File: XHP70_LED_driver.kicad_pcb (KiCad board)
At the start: 2 copper layers, 17 x 17 mm, 24 parts, among them U1 TPS61088, U2 INA181

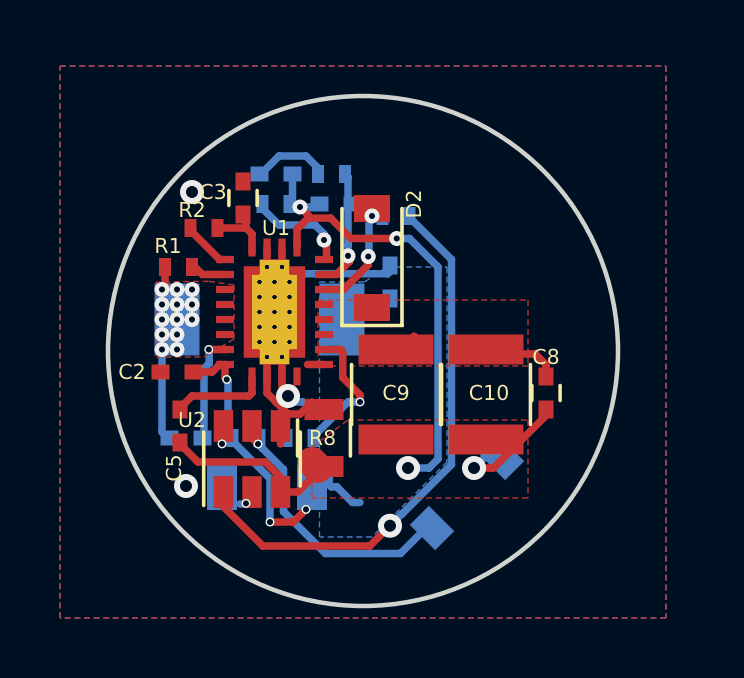
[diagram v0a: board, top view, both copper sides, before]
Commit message: added microcontroller
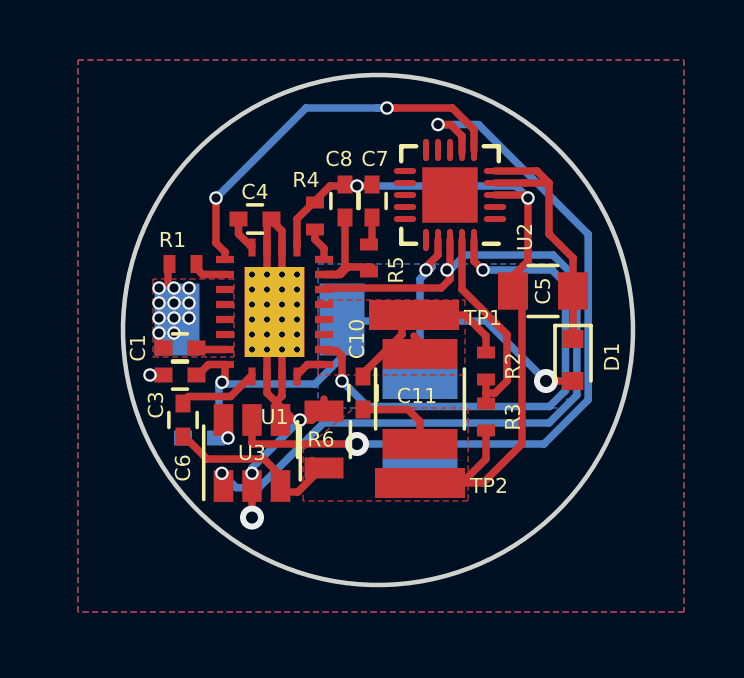
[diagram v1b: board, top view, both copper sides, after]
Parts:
- removed D2: D_Zener, Diodes_SMD:D_SOD-123
- removed R7: 10k, Resistors_SMD:R_0402_NoSilk
- removed R8: 12m, Resistors_SMD:R_0805
- added TP1: TestPoint, Misc:flashlight_batt, F.Cu at (104.4, 57.1)
- added TP2: TestPoint, Misc:flashlight_batt, F.Cu at (104.6, 62.7)
- added U3: INA181, TO_SOT_Packages_SMD:SOT-23-6, F.Cu at (99.0, 61.7)
- C1: value 10u -> 100n; footprint Capacitors_SMD:C_1206 -> Capacitors_SMD:C_0402; moved to F.Cu
- C10: value 100u -> 100n; footprint Capacitors_SMD:C_1210 -> Capacitors_SMD:C_0402
- C11: value 10u -> 100u; footprint Capacitors_SMD:C_0402 -> Capacitors_SMD:C_1210; moved to F.Cu
- C2: value 100n -> 10u; footprint Capacitors_SMD:C_0402_NoSilk -> Capacitors_SMD:C_1210; moved to B.Cu
- C3: value 10u -> 100n
- C4: value 100n -> 10u; moved to F.Cu
- C5: value 10n -> 47u; footprint Capacitors_SMD:C_0402_NoSilk -> Capacitors_SMD:C_0805
- C6: value C -> 10n; footprint Capacitors_SMD:C_0402_NoSilk -> Capacitors_SMD:C_0402; moved to F.Cu
- C7: footprint Capacitors_SMD:C_0402_NoSilk -> Capacitors_SMD:C_0402; moved to F.Cu
- C8: value 100n -> C
- C9: value 100u -> 10u; footprint Capacitors_SMD:C_1210 -> Capacitors_SMD:C_0402; moved to B.Cu
- D1: value D_Zener -> D_Schottky; footprint Diodes_SMD:D_SOD-123 -> Diodes_SMD:D_SOD-523; moved to F.Cu
- R3: value 10k -> 100k; moved to F.Cu
- R4: moved to F.Cu
- R5: value 100k -> R; moved to F.Cu
- R6: value R -> 12m; footprint Resistors_SMD:R_0402_NoSilk -> Resistors_SMD:R_0805; moved to F.Cu
- U2: value INA181 -> ATtiny816_(QFN20); footprint TO_SOT_Packages_SMD:SOT-23-6 -> Housings_DFN_QFN:UQFN-20-1EP_3x3mm_Pitch0.4mm
- moved C5 12.9 mm to (108.7, 56.3), turned to 0 degrees
- moved U2 11.0 mm to (105.6, 53.1), turned to 180 degrees
- moved R2 10.5 mm to (106.8, 58.8), turned to 90 degrees
- moved C8 9.27 mm to (102.1, 53.3), turned to 270 degrees
- moved R6 8.85 mm to (101.4, 61.2), turned to 90 degrees
- moved C6 8.77 mm to (96.7, 60.6), turned to 90 degrees
- moved C2 8.32 mm to (104.6, 60.9), turned to 90 degrees
- moved R3 8.03 mm to (106.8, 60.5), turned to 90 degrees
- moved C4 7.65 mm to (99.1, 53.9)
- moved R4 7.42 mm to (101.1, 53.8), turned to 270 degrees
- moved C9 6.71 mm to (97.2, 61.2), turned to 0 degrees
- moved C3 6.26 mm to (96.6, 59.1), turned to 0 degrees
- moved D1 5.67 mm to (109.7, 58.6), turned to 270 degrees
- moved C1 5.44 mm to (96.6, 58.2), turned to 180 degrees
- moved C10 4.10 mm to (102.7, 59.7)
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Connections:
- C1 pad 1: GND -> Net-(C1-Pad1)
- C1 pad 2: +BATT -> Net-(C1-Pad2)
- C11 pad 1: GND -> /LED_K
- C11 pad 2: +BATT -> /LED_A
- C3 pad 2: Net-(C3-Pad2) -> +BATT
- C4 pad 1: Net-(C4-Pad1) -> GND
- C8 pad 2: /LED_A -> Net-(C8-Pad2)
- C9 pad 1: /LED_K -> GND
- C9 pad 2: /LED_A -> +BATT
- D1 pad 1: Net-(D1-Pad1) -> Net-(C5-Pad2)
- D1 pad 2: /LED_K -> +BATT
- L1 pad 1: Net-(C4-Pad2) -> Net-(C1-Pad2)
- R1 pad 2: Net-(C4-Pad2) -> Net-(C1-Pad2)
- R2 pad 1: Net-(R2-Pad1) -> /ADC_VOUT
- R2 pad 2: Net-(C3-Pad2) -> /LED_A
- R3 pad 1: Net-(D1-Pad1) -> /LED_K
- R3 pad 2: +BATT -> /ADC_VOUT
- R4 pad 1: GND -> /LED_K
- R5 pad 1: /LED_K -> Net-(C8-Pad2)
- R5 pad 2: Net-(R5-Pad2) -> Net-(C7-Pad2)
- R6 pad 1: Net-(C7-Pad2) -> /LED_K
- R6 pad 2: Net-(C6-Pad2) -> GND
- U1 pad 1: Net-(C3-Pad2) -> Net-(C4-Pad2)
- U1 pad 10: Net-(C5-Pad2) -> Net-(C6-Pad2)
- U1 pad 13: Net-(R4-Pad2) -> /MODE
- U1 pad 17: Net-(D2-Pad2) -> /ADC_IOUT
- U1 pad 18: Net-(C7-Pad2) -> Net-(C8-Pad2)
- U1 pad 19: Net-(R5-Pad2) -> Net-(R4-Pad2)
- U1 pad 2: Net-(R2-Pad1) -> /ENABLE
- U1 pad 4: Net-(C4-Pad2) -> Net-(C1-Pad2)
- U1 pad 5: Net-(C4-Pad2) -> Net-(C1-Pad2)
- U1 pad 6: Net-(C4-Pad2) -> Net-(C1-Pad2)
- U1 pad 7: Net-(C4-Pad2) -> Net-(C1-Pad2)
- U1 pad 8: Net-(C4-Pad1) -> Net-(C1-Pad1)
- U2 pad 2: GND -> Net-(U2-Pad2)
- U2 pad 4: GND -> Net-(C5-Pad2)
- U2 pad 5: Net-(D1-Pad1) -> Net-(C5-Pad2)
- U2 pad 6: +BATT -> /ENABLE
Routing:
- net /ADC_IOUT: track 0.00 -> 28.0 mm, vias 0 -> 2
- net /DAC_OUT: track 0.00 -> 26.2 mm, vias 0 -> 2
- net Net-(U2-Pad1): track 18.7 -> 0.00 mm, vias 1 -> 0
- net /MODE: track 0.00 -> 17.1 mm, vias 0 -> 2
- net +BATT: track 10.9 -> 23.9 mm
- net /ENABLE: track 0.00 -> 13.0 mm, vias 0 -> 2
- net Net-(D1-Pad1): track 9.78 -> 0.00 mm, vias 1 -> 0
- net /LED_K: track 27.2 -> 36.2 mm, vias 4 -> 2
- net /ADC_VOUT: track 0.00 -> 6.94 mm
- net Net-(C5-Pad2): track 3.16 -> 9.20 mm
- net Net-(C8-Pad2): track 0.00 -> 4.01 mm
- net Net-(C7-Pad2): track 4.39 -> 0.40 mm, vias 1 -> 0
- net Net-(D2-Pad2): track 3.73 -> 0.00 mm, vias 2 -> 0
- net Net-(C4-Pad1): track 3.56 -> 0.00 mm, vias 1 -> 0
- net Net-(R4-Pad2): track 4.67 -> 1.17 mm, vias 1 -> 0
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- added copper zone on F.Cu, net Net-(C1-Pad2)
- removed copper zone on F.Cu, net Net-(C4-Pad2)
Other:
- net class Default: clearance 0.2 -> 0.127
- rule trace_clearance: 0.2 -> 0.127
- rule trace_min: 0.2 -> 0.0889
- rule via_min_size: 0.2 -> 0.45
